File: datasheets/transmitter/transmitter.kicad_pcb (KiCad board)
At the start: 2 copper layers, 8 parts, among them CON1 AVR-ISP-6, IC1 ATTINY85-P, Q1 Q_NPN_EBC

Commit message: Kicad PCB layout
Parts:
- removed REF**: Pin_Header_Straight_1x02, Pin_Headers:Pin_Header_Straight_1x02
- removed REF**: SolderWirePad_2x_0-8mmDrill, Wire_Pads:SolderWirePad_2x_0-8mmDrill
- added ?: , Wire_Pads:SolderWirePad_single_0-8mmDrill, F.Cu at (128.3, 118.1)
- added ?: , Wire_Pads:SolderWirePad_single_0-8mmDrill, F.Cu at (128.3, 108.6)
- ?: renamed from CON1; value AVR-ISP-6 -> (none)
- moved R2 8.52 mm to (114.9, 121.3), turned to 90 degrees
- moved Q1 6.98 mm to (114.3, 110.5)
- moved D1 4.07 mm to (110.5, 121.3)
- moved R1 2.54 mm to (109.9, 114.3), turned to 90 degrees
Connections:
- net +5V renamed VCC
- IC1 pad 2: Net-(IC1-Pad2) -> (no net)
- IC1 pad 3: Net-(IC1-Pad3) -> (no net)
- R1 pad 2: Net-(IC1-Pad2) -> Net-(CON1-Pad1)
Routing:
- net Net-(CON1-Pad1): track 8.04 -> 40.1 mm
- net VCC: track 40.4 -> 21.9 mm
- net Net-(D1-Pad1): track 9.94 -> 4.45 mm
- net Net-(IC1-Pad2): track 5.13 -> 0.00 mm
- net Net-(D1-Pad2): track 13.3 -> 9.83 mm
- net (no net): track 0.00 -> 2.54 mm
- net Net-(Q1-Pad2): track 7.40 -> 8.41 mm

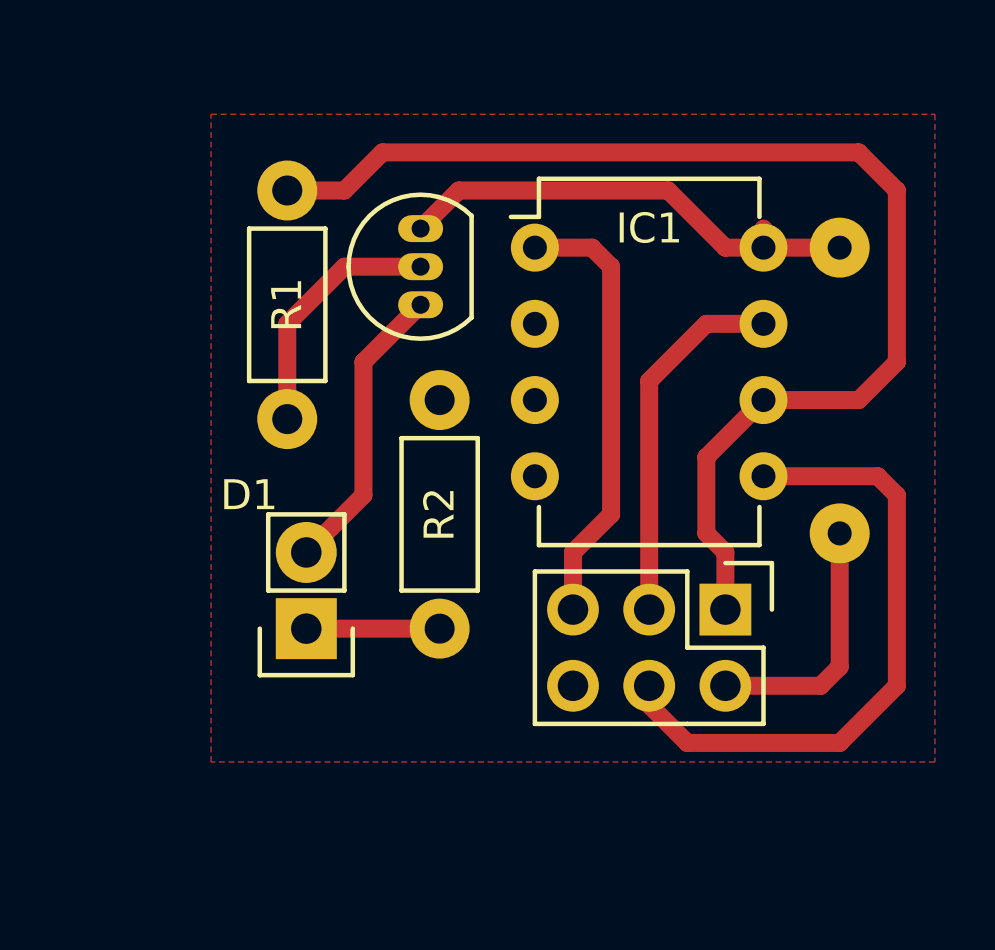
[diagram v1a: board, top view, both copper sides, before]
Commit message: Reroute LED and transistor. Remove backup files from git.
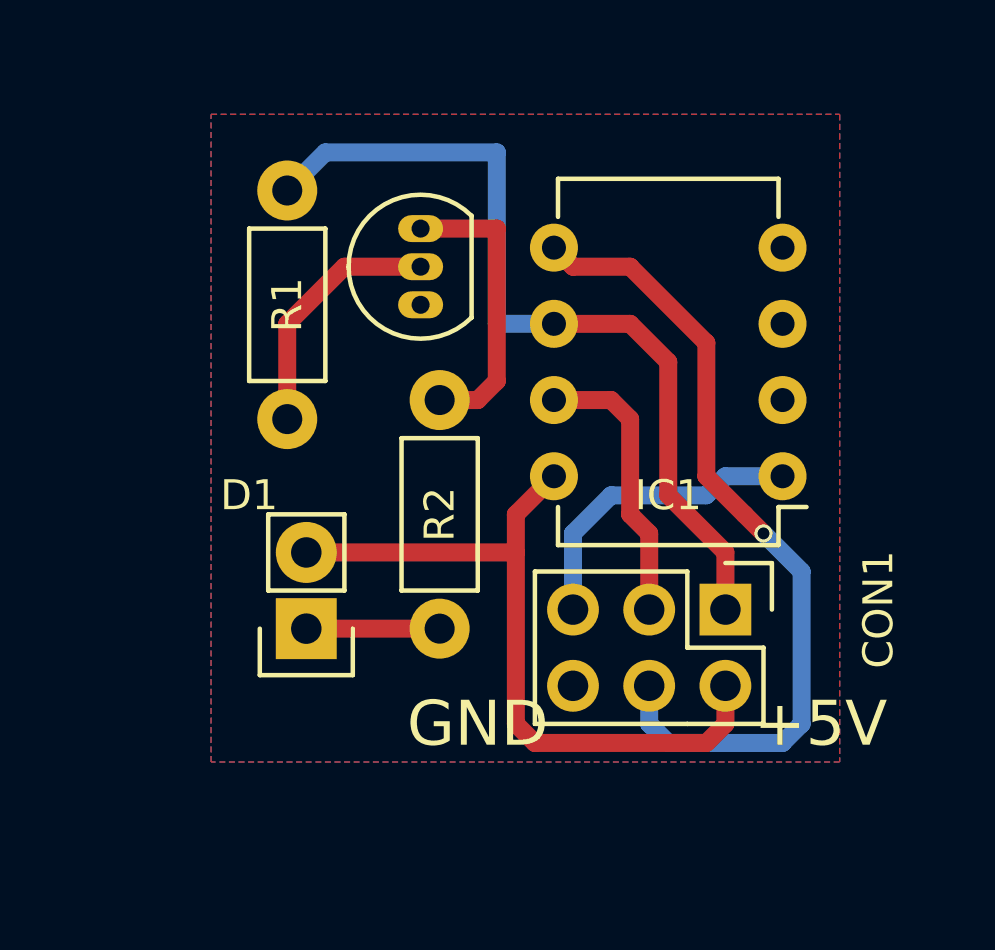
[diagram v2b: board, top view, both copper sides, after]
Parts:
- removed ?: , Pin_Headers:Pin_Header_Straight_2x03
- removed ? (x2): , Wire_Pads:SolderWirePad_single_0-8mmDrill
- added CON1: AVR-ISP-6, Pin_Headers:Pin_Header_Straight_2x03, F.Cu at (124.5, 120.7)
- R2: value 56 -> 39
- moved IC1 11.2 mm to (126.4, 116.2), turned to 180 degrees
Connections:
- D1 pad 2: Net-(D1-Pad2) -> VCC
- Q1 pad 1: Net-(D1-Pad2) -> GND
- Q1 pad 3: VCC -> Net-(Q1-Pad3)
- R2 pad 2: GND -> Net-(Q1-Pad3)
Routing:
- net Net-(CON1-Pad1): track 40.1 -> 28.5 mm
- net Net-(D1-Pad2): track 9.83 -> 0.00 mm
- net Net-(Q1-Pad3): track 0.00 -> 9.79 mm
- net Net-(CON1-Pad4): track 21.3 -> 27.3 mm, vias 0 -> 1
- net Net-(CON1-Pad5): track 14.8 -> 10.3 mm
- net VCC: track 21.9 -> 25.2 mm
- net Net-(CON1-Pad3): track 12.2 -> 9.42 mm
- net (no net): track 2.54 -> 0.00 mm
- added copper zone on B.Cu, net GND
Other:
- board text added: "+5V"
- board text added: "GND"
